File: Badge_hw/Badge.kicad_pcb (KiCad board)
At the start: 2 copper layers, 143 parts, among them Q1 IRLML9303, Q2 BC848

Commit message: +antenna
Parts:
- added D7: ANT, ANT_868_INV_F:ANTENNA_868_INV_F, F.Cu at (222.6, 22.6)
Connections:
- BLN1 pad 2: GNDS -> Net-(BLN1-Pad2)
- BLN1 pad 5: GNDS -> Net-(BLN1-Pad2)
- BLN1 pad 6: GNDS -> Net-(BLN1-Pad2)
- C14 pad 2: GNDS -> Net-(C14-Pad2)
- C15 pad 2: GNDS -> Net-(C15-Pad2)
- C16 pad 2: GNDS -> Net-(C16-Pad2)
- C19 pad 2: GNDS -> Net-(C15-Pad2)
- C20 pad 2: GNDS -> Net-(C20-Pad2)
- C3 pad 2: GNDS -> Net-(C15-Pad2)
- C31 pad 2: GNDS -> Net-(C31-Pad2)
- C32 pad 2: GNDS -> Net-(C32-Pad2)
- C33 pad 2: GNDS -> Net-(C33-Pad2)
- C34 pad 2: GNDS -> Net-(C34-Pad2)
- C35 pad 2: GNDS -> Net-(C35-Pad2)
- C36 pad 2: GNDS -> Net-(C36-Pad2)
- C37 pad 2: GNDS -> Net-(C37-Pad2)
- C38 pad 2: GNDS -> Net-(C38-Pad2)
- C39 pad 2: GNDS -> Net-(C39-Pad2)
- C40 pad 2: GNDS -> Net-(C40-Pad2)
- C41 pad 2: GNDS -> Net-(C41-Pad2)
- C42 pad 2: GNDS -> Net-(C42-Pad2)
- C43 pad 2: GNDS -> Net-(C43-Pad2)
- C44 pad 2: GNDS -> Net-(C44-Pad2)
- C45 pad 2: GNDS -> Net-(C45-Pad2)
- C47 pad 2: GNDS -> Net-(C47-Pad2)
- C48 pad 2: GNDS -> Net-(C48-Pad2)
- C50 pad 1: GNDS -> Net-(C50-Pad1)
- C51 pad 2: GNDS -> Net-(C51-Pad2)
- C53 pad 2: GNDS -> Net-(C53-Pad2)
- C54 pad 2: GNDS -> Net-(C54-Pad2)
- C55 pad 2: GNDS -> Net-(C55-Pad2)
- C56 pad 2: GNDS -> Net-(C56-Pad2)
- C57 pad 2: GNDS -> Net-(C57-Pad2)
- C59 pad 2: GNDS -> Net-(C59-Pad2)
- C60 pad 2: GNDS -> Net-(C60-Pad2)
- C61 pad 2: GNDS -> Net-(C61-Pad2)
- C62 pad 2: GNDS -> Net-(C62-Pad2)
- C63 pad 2: GNDS -> Net-(C63-Pad2)
- C64 pad 2: GNDS -> Net-(C64-Pad2)
- C65 pad 2: GNDS -> Net-(C65-Pad2)
- C66 pad 2: GNDS -> Net-(C66-Pad2)
- C9 pad 2: GNDS -> Net-(C15-Pad2)
- D2 pad C: GNDS -> Net-(D2-PadC)
- D4 pad 1: GNDS -> Net-(D4-Pad1)
- D4 pad 2: GNDS -> Net-(D4-Pad1)
- D4 pad 3: GNDS -> Net-(D4-Pad1)
- DA1 pad 4: GNDS -> Net-(DA1-Pad4)
- DD1 pad 10: GNDS -> Net-(DD1-Pad10)
- DD1 pad 3: GNDS -> Net-(DD1-Pad3)
- DD1 pad 9: GNDS -> Net-(DD1-Pad9)
- DD2 pad 11: GNDS -> Net-(DD2-Pad11)
- DD2 pad 12: GNDS -> Net-(DD2-Pad11)
- DD2 pad 13: GNDS -> Net-(DD2-Pad11)
- DD2 pad 14: GNDS -> Net-(DD2-Pad11)
- DD2 pad 15: GNDS -> Net-(DD2-Pad15)
- DD2 pad 16: GNDS -> Net-(DD2-Pad15)
- DD2 pad 34: GNDS -> Net-(DD2-Pad34)
- DD2 pad 7: GNDS -> Net-(DD2-Pad11)
- DD2 pad 9: GNDS -> Net-(DD2-Pad11)
- DD4 pad 10: GNDS -> Net-(DD4-Pad10)
- DD4 pad 19: GNDS -> Net-(DD4-Pad19)
- DD4 pad 20: GNDS -> Net-(DD4-Pad20)
- DD4 pad 27: GNDS -> Net-(DD4-Pad10)
- DD4 pad 49: GNDS -> Net-(DD4-Pad10)
- DD4 pad 74: GNDS -> Net-(DD4-Pad10)
- DD4 pad 99: GNDS -> Net-(DD4-Pad10)
- DD5 pad 16: GNDS -> Net-(DD5-Pad16)
- DD5 pad 19: GNDS -> Net-(DD5-Pad16)
- DD5 pad PAD: GNDS -> Net-(DD5-PadPAD)
- L6 pad 2: GNDS -> Net-(L6-Pad2)
- Q2 pad 2: GNDS -> Net-(Q2-Pad2)
- R34 pad 1: GNDS -> Net-(R34-Pad1)
- R35 pad 2: GNDS -> Net-(R35-Pad2)
- R36 pad 1: GNDS -> Net-(R36-Pad1)
- R40 pad 2: GNDS -> Net-(R40-Pad2)
- R42 pad 1: GNDS -> Net-(R42-Pad1)
- R46 pad 2: GNDS -> Net-(R46-Pad2)
- SA2 pad 1: GNDS -> Net-(SA2-Pad1)
- XL3 pad 6: GNDS -> Net-(XL3-Pad6)
- XL3 pad H: GNDS -> Net-(XL3-PadH)
- XTAL1 pad H: GNDS -> Net-(XTAL1-PadH)
- XTAL2 pad H: GNDS -> Net-(XTAL2-PadH)

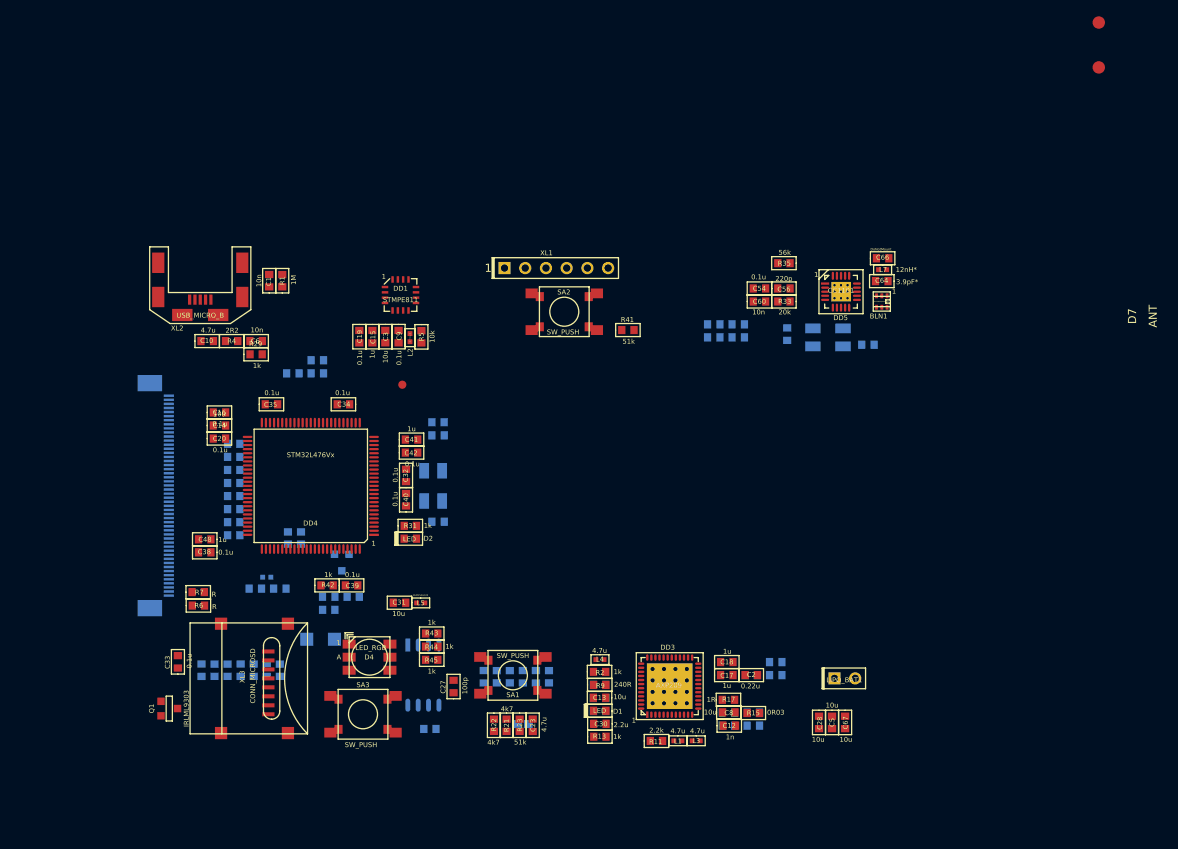
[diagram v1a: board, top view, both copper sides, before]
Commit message: * pcb redraw + barometer scheme
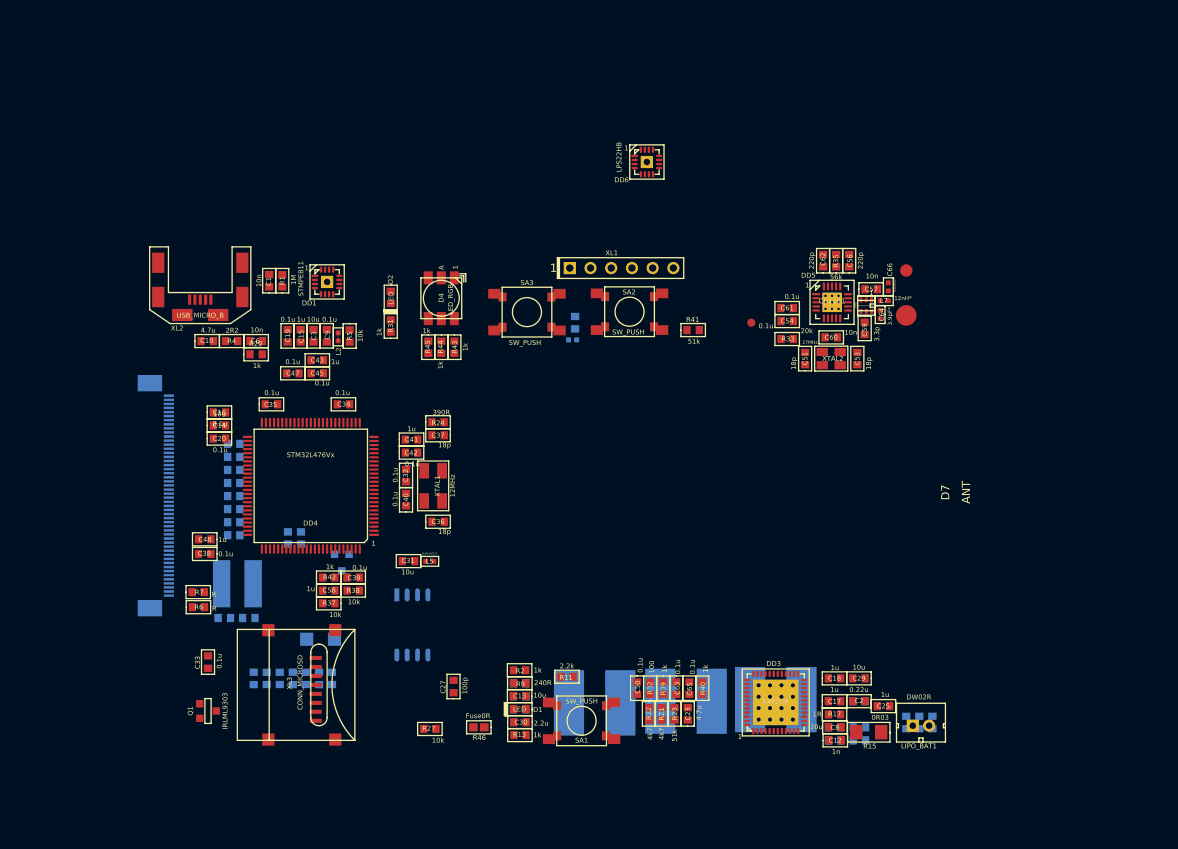
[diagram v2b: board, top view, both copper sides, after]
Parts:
- added C68: 0.1u, Capacitors:CAP_0603, B.Cu at (158.4, 59.4)
- added DD6: LPS22HB, QFN_DFN:QFN16_4x4_H, F.Cu at (167.2, 39.7)
- added L8: BLM15AG102, Inductors:IND_0402, B.Cu at (158.1, 61.5)
- C25, C29, C36, C37, C43, C45, C47, C50, C51, C53, C57, C58, C59, C61, C62, C63, C65, R24, R27, R32, R37, R38, R39, R40, R46, XTAL1: moved to F.Cu
- C28, C5, C67: moved to B.Cu
- C64, C66: footprint Capacitors:CAP_0603 -> Capacitors:CAP_0402
- D7: footprint ANT_868_INV_F:ANTENNA_868_INV_F -> ANT_868_INV_F:ANTENNA_868_INV_F_SHARP
- DD1: footprint LGA:16_4X4_P065 -> QFN_DFN:QFN16_4x4_H
- L1, L3, L4: footprint Inductors:IND_0402 -> Inductors:SDR0805; moved to B.Cu
- L6: footprint Inductors:IND_0402 -> Inductors:IND_SDR0604
- LIPO_BAT1: footprint Connectors:PLS-2 -> Connectors:WB-02(MW-2M)
- R15: footprint Resistors:RES_0603 -> Resistors:RES_1206
- XTAL2: footprint Quartz:0503x4-4 -> Quartz:03225C4; moved to F.Cu
- moved SA3 53.2 mm to (152.5, 58.1)
- moved D4 44.9 mm to (142.0, 56.4), turned to 270 degrees
- moved TP1 43.4 mm to (180.0, 59.4)
- moved R45 38.3 mm to (140.4, 62.4), turned to 270 degrees
- moved D7 38.0 mm to (199.8, 53.0)
- moved R44 36.7 mm to (142.0, 62.4), turned to 270 degrees
- moved R43 35.2 mm to (143.6, 62.4), turned to 270 degrees
- moved D2 29.7 mm to (135.8, 56.3), turned to 270 degrees
- moved R31 24.6 mm to (135.8, 59.8), turned to 90 degrees
- moved L4 22.1 mm to (183.0, 105.6), turned to 90 degrees
- moved C57 19.8 mm to (194.7, 55.3)
- moved C23 19.1 mm to (172.2, 107.3)
- moved R21 19.1 mm to (169.0, 107.3)
- moved R22 19.1 mm to (167.4, 107.3)
- moved R23 19.1 mm to (170.6, 107.3)
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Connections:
- C1 pad 2: GND -> Net-(C1-Pad2)
- C10 pad 1: GND -> Net-(C10-Pad1)
- C11 pad 2: GND -> Net-(C11-Pad2)
- C12 pad 2: GND -> Net-(C12-Pad2)
- C13 pad 2: GND -> Net-(C13-Pad2)
- C17 pad 2: GND -> Net-(C17-Pad2)
- C18 pad 2: GND -> Net-(C18-Pad2)
- C2 pad 2: GND -> Net-(C2-Pad2)
- C21 pad 2: GND -> Net-(C21-Pad2)
- C22 pad 2: GND -> Net-(C22-Pad2)
- C23 pad 1: +3V3 -> +3V3_120mA
- C23 pad 2: GND -> Net-(C23-Pad2)
- C24 pad 2: GND -> Net-(C24-Pad2)
- C25 pad 2: GND -> Net-(C25-Pad2)
- C26 pad 2: GND -> Net-(C26-Pad2)
- C27 pad 2: GND -> Net-(C27-Pad2)
- C28 pad 2: GND -> Net-(C28-Pad2)
- C29 pad 1: GND -> Net-(C29-Pad1)
- C30 pad 2: GND -> Net-(C30-Pad2)
- C4 pad 2: GND -> Net-(C4-Pad2)
- C5 pad 2: GND -> Net-(C5-Pad2)
- C6 pad 2: GND -> Net-(C6-Pad2)
- C67 pad 2: GND -> Net-(C5-Pad2)
- C7 pad 2: GND -> Net-(C7-Pad2)
- C8 pad 2: GND -> Net-(C8-Pad2)
- DD2 pad 1: +3V3 -> +3V3_120mA
- DD2 pad 43: GND -> Net-(DD2-Pad43)
- DD2 pad 48: GND -> Net-(DD2-Pad43)
- DD2 pad 49: GND -> Net-(DD2-Pad43)
- DD2 pad 50: GND -> Net-(DD2-Pad43)
- DD3 pad 12: +3V3 -> +3V3_120mA
- DD3 pad 16: GND -> Net-(DD3-Pad16)
- DD3 pad 22: GND -> Net-(DD3-Pad22)
- DD3 pad 46: GND -> Net-(DD3-Pad46)
- DD3 pad 6: GND -> Net-(DD3-Pad6)
- DD3 pad 9: GND -> Net-(DD3-Pad9)
- DD3 pad PAD: GND -> Net-(DD3-PadPAD)
- DD4 pad 81: Net-(DD4-Pad81) -> /PRESSURE_INT
- LIPO_BAT1 pad 2: GND -> Net-(C5-Pad2)
- R1 pad 2: GND -> Net-(R1-Pad2)
- R11 pad 1: GND -> Net-(R11-Pad1)
- R3 pad 2: GND -> Net-(R3-Pad2)
- R46 pad 1: GND -> Net-(R46-Pad1)
- R6 pad 2: +3V3 -> +3V3_120mA
- R7 pad 2: +3V3 -> +3V3_120mA
- R9 pad 1: GND -> Net-(R9-Pad1)
- SA1 pad 2: GND -> Net-(SA1-Pad2)
- XL1 pad 3: GND -> Net-(XL1-Pad3)
- XL2 pad 4: GND -> Net-(XL2-Pad4)
- XL2 pad 5: GND -> Net-(XL2-Pad4)

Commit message: * schematic, footprints
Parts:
- C44: value 150pF -> 150p
- C49: value 100pF -> 100p
- C64: value 3.9pF* -> 3.9p*
- DA1: footprint SO_DIL_TSSOP:SO8_208MIL -> SOT:SOT23-8
- DD6: footprint QFN_DFN:QFN16_4x4_H -> LGA:10_2X2
- L1, L3, L4: value 4.7u -> 4.7uH; footprint Inductors:SDR0805 -> Inductors:IND_SDR0604
- L6: footprint Inductors:IND_SDR0604 -> Inductors:IND_1812
- R15: footprint Resistors:RES_1206 -> Resistors:RES_2512
- moved DD6 40.8 mm to (136.0, 66.0)
- moved LIPO_BAT1 9.95 mm to (192.2, 103.8)
- moved C25 9.11 mm to (187.6, 103.4)
- moved R46 9.02 mm to (137.6, 108.4)
- moved DD3 9.01 mm to (174.0, 106.4)
- moved D1 8.80 mm to (142.8, 106.8)
- moved R9 8.80 mm to (142.8, 103.6)
- moved C13 8.80 mm to (142.8, 105.2)
- moved C24 8.80 mm to (142.8, 103.6)
- moved C26 8.80 mm to (142.8, 105.2)
- moved C30 8.80 mm to (142.8, 108.4)
- moved C7 8.80 mm to (142.8, 106.8)
- moved R13 8.80 mm to (142.8, 110.0)
- moved R2 8.80 mm to (142.8, 102.0)
- moved C17 8.61 mm to (181.6, 106.2)
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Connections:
- BLN1 pad 2: Net-(BLN1-Pad2) -> GNDS
- BLN1 pad 5: Net-(BLN1-Pad2) -> GNDS
- BLN1 pad 6: Net-(BLN1-Pad2) -> GNDS
- C1 pad 2: Net-(C1-Pad2) -> GNDA
- C10 pad 1: Net-(C10-Pad1) -> GNDA
- C11 pad 2: Net-(C11-Pad2) -> GNDA
- C12 pad 2: Net-(C12-Pad2) -> GNDA
- C13 pad 2: Net-(C13-Pad2) -> GNDA
- C14 pad 2: Net-(C14-Pad2) -> GNDS
- C16 pad 2: Net-(C16-Pad2) -> GNDS
- C17 pad 2: Net-(C17-Pad2) -> GNDA
- C18 pad 2: Net-(C18-Pad2) -> GNDA
- C2 pad 2: Net-(C2-Pad2) -> GNDA
- C20 pad 2: Net-(C20-Pad2) -> GNDS
- C21 pad 2: Net-(C21-Pad2) -> GNDA
- C22 pad 2: Net-(C22-Pad2) -> GNDA
- C23 pad 2: Net-(C23-Pad2) -> GNDA
- C24 pad 2: Net-(C24-Pad2) -> GNDA
- C25 pad 2: Net-(C25-Pad2) -> GNDA
- C26 pad 2: Net-(C26-Pad2) -> GNDA
- C27 pad 2: Net-(C27-Pad2) -> GNDA
- C28 pad 2: Net-(C28-Pad2) -> GNDA
- C29 pad 1: Net-(C29-Pad1) -> GNDA
- C30 pad 2: Net-(C30-Pad2) -> GNDA
- C31 pad 2: Net-(C31-Pad2) -> GNDS
- C32 pad 2: Net-(C32-Pad2) -> GNDS
- C33 pad 2: Net-(C33-Pad2) -> GNDS
- C34 pad 2: Net-(C34-Pad2) -> GNDS
- C35 pad 2: Net-(C35-Pad2) -> GNDS
- C36 pad 2: Net-(C36-Pad2) -> GNDS
- C37 pad 2: Net-(C37-Pad2) -> GNDS
- C38 pad 2: Net-(C38-Pad2) -> GNDS
- C39 pad 2: Net-(C39-Pad2) -> GNDS
- C4 pad 2: Net-(C4-Pad2) -> GNDA
- C40 pad 2: Net-(C40-Pad2) -> GNDS
- C41 pad 2: Net-(C41-Pad2) -> GNDS
- C42 pad 2: Net-(C42-Pad2) -> GNDS
- C43 pad 2: Net-(C43-Pad2) -> GNDS
- C44 pad 2: Net-(C44-Pad2) -> GNDS
- C45 pad 2: Net-(C45-Pad2) -> GNDS
- C47 pad 2: Net-(C47-Pad2) -> GNDS
- C48 pad 2: Net-(C48-Pad2) -> GNDS
- C5 pad 2: Net-(C5-Pad2) -> GNDA
- C50 pad 1: Net-(C50-Pad1) -> GNDS
- C51 pad 2: Net-(C51-Pad2) -> GNDS
- C53 pad 2: Net-(C53-Pad2) -> GNDS
- C54 pad 2: Net-(C54-Pad2) -> GNDS
- C55 pad 2: Net-(C55-Pad2) -> GNDS
- C56 pad 2: Net-(C56-Pad2) -> GNDS
- C57 pad 2: Net-(C57-Pad2) -> GNDS
- C59 pad 2: Net-(C59-Pad2) -> GNDS
- C6 pad 2: Net-(C6-Pad2) -> GNDA
- C60 pad 2: Net-(C60-Pad2) -> GNDS
- C61 pad 2: Net-(C61-Pad2) -> GNDS
- C62 pad 2: Net-(C62-Pad2) -> GNDS
- C63 pad 2: Net-(C63-Pad2) -> GNDS
- C64 pad 2: Net-(C64-Pad2) -> GNDS
- C65 pad 2: Net-(C65-Pad2) -> GNDS
- C66 pad 2: Net-(C66-Pad2) -> GNDS
- C67 pad 2: Net-(C5-Pad2) -> GNDA
- C68 pad 2: Net-(C68-Pad2) -> GNDS
- C7 pad 2: Net-(C7-Pad2) -> GNDA
- C8 pad 2: Net-(C8-Pad2) -> GNDA
- D2 pad C: Net-(D2-PadC) -> GNDS
- D4 pad 1: Net-(D4-Pad1) -> GNDS
- D4 pad 2: Net-(D4-Pad1) -> GNDS
- D4 pad 3: Net-(D4-Pad1) -> GNDS
- D7 pad GND: Net-(D7-PadGND) -> GNDS
- DD1 pad 10: Net-(DD1-Pad10) -> GNDS
- DD1 pad 3: Net-(DD1-Pad3) -> GNDS
- DD1 pad 9: Net-(DD1-Pad9) -> GNDS
- DD2 pad 11: Net-(DD2-Pad11) -> GNDS
- DD2 pad 12: Net-(DD2-Pad11) -> GNDS
- DD2 pad 13: Net-(DD2-Pad11) -> GNDS
- DD2 pad 14: Net-(DD2-Pad11) -> GNDS
- DD2 pad 15: Net-(DD2-Pad15) -> GNDS
- DD2 pad 16: Net-(DD2-Pad15) -> GNDS
- DD2 pad 34: Net-(DD2-Pad34) -> GNDS
- DD2 pad 43: Net-(DD2-Pad43) -> GNDA
- DD2 pad 48: Net-(DD2-Pad43) -> GNDA
- DD2 pad 49: Net-(DD2-Pad43) -> GNDA
- DD2 pad 50: Net-(DD2-Pad43) -> GNDA
- DD2 pad 7: Net-(DD2-Pad11) -> GNDS
- DD2 pad 9: Net-(DD2-Pad11) -> GNDS
- DD3 pad 16: Net-(DD3-Pad16) -> GNDA
- DD3 pad 22: Net-(DD3-Pad22) -> GNDA
- DD3 pad 46: Net-(DD3-Pad46) -> GNDA
- DD3 pad 6: Net-(DD3-Pad6) -> GNDA
- DD3 pad 9: Net-(DD3-Pad9) -> GNDA
- DD3 pad PAD: Net-(DD3-PadPAD) -> GNDA
- DD4 pad 10: Net-(DD4-Pad10) -> GNDS
- DD4 pad 19: Net-(DD4-Pad19) -> GNDS
- DD4 pad 20: Net-(DD4-Pad20) -> GNDS
- DD4 pad 27: Net-(DD4-Pad10) -> GNDS
- DD4 pad 49: Net-(DD4-Pad10) -> GNDS
- DD4 pad 74: Net-(DD4-Pad10) -> GNDS
- DD4 pad 99: Net-(DD4-Pad10) -> GNDS
- DD5 pad 16: Net-(DD5-Pad16) -> GNDS
- DD5 pad 19: Net-(DD5-Pad16) -> GNDS
- DD5 pad PAD: Net-(DD5-PadPAD) -> GNDS
- DD6 pad 3: Net-(DD6-Pad3) -> GNDS
- DD6 pad 5: Net-(DD6-Pad3) -> GNDS
- DD6 pad 8: Net-(DD6-Pad8) -> GNDS
- DD6 pad 9: Net-(DD6-Pad8) -> GNDS
- L6 pad 2: Net-(L6-Pad2) -> GNDS
- LIPO_BAT1 pad 2: Net-(C5-Pad2) -> GNDA
- Q2 pad 2: Net-(Q2-Pad2) -> GNDS
- R1 pad 2: Net-(R1-Pad2) -> GNDA
- R11 pad 1: Net-(R11-Pad1) -> GNDA
- R3 pad 2: Net-(R3-Pad2) -> GNDA
- R34 pad 1: Net-(R34-Pad1) -> GNDS
- R35 pad 2: Net-(R35-Pad2) -> GNDS
- R36 pad 1: Net-(R36-Pad1) -> GNDS
- R40 pad 2: Net-(R40-Pad2) -> GNDS
- R42 pad 1: Net-(R42-Pad1) -> GNDS
- R46 pad 1: Net-(R46-Pad1) -> GNDA
- R46 pad 2: Net-(R46-Pad2) -> GNDS
- R9 pad 1: Net-(R9-Pad1) -> GNDA
- SA1 pad 2: Net-(SA1-Pad2) -> GNDA
- SA2 pad 1: Net-(SA2-Pad1) -> GNDS
- XL1 pad 3: Net-(XL1-Pad3) -> GNDA
- XL2 pad 4: Net-(XL2-Pad4) -> GNDA
- XL2 pad 5: Net-(XL2-Pad4) -> GNDA
- XL3 pad 6: Net-(XL3-Pad6) -> GNDS
- XL3 pad H: Net-(XL3-PadH) -> GNDS
- XTAL1 pad H: Net-(XTAL1-PadH) -> GNDS
- XTAL2 pad H: Net-(XTAL2-PadH) -> GNDS
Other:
- board outline added: 114 x 62 mm

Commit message: +pcb
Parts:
- C1, C10, C13, C17, C18, C2, C23, C25, C27, C29, C30, C6, C63, C65, D1, DD3, LIPO_BAT1, R1, R11, R13, R15, R17, R2, R21, R22, R23, R29, R39, R4, R40, R46, R9, SA2, SA3, XL2: moved to B.Cu
- C11, C4, C44, C46, C49, C52, C55, D3, DA1, L1, L3, L4, L6, Q2, R25, R26, R28, R30, R34, R36: moved to F.Cu
- moved C44 72.0 mm to (189.0, 109.7)
- moved C46 72.0 mm to (186.0, 109.7)
- moved R15 66.0 mm to (130.8, 81.6)
- moved C25 64.9 mm to (123.0, 97.4)
- moved C67 63.2 mm to (134.5, 88.0), turned to 0 degrees
- moved C49 62.8 mm to (181.2, 111.1), turned to 0 degrees
- moved C5 62.4 mm to (134.5, 86.4), turned to 0 degrees
- moved C19 61.9 mm to (162.6, 108.7)
- moved C28 61.5 mm to (134.5, 84.9), turned to 0 degrees
- moved C15 61.1 mm to (162.6, 108.9)
- moved R28 61.0 mm to (181.2, 109.5), turned to 0 degrees
- moved R3 59.4 mm to (128.2, 105.2), turned to 270 degrees
- moved C22 59.3 mm to (125.6, 89.8)
- moved R30 59.2 mm to (181.2, 107.9), turned to 0 degrees
- moved C31 58.8 mm to (194.6, 104.4)
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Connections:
- DD3 pad 2: /SCK -> /SCL
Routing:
- net GNDA: track 0.00 -> 120.4 mm, vias 0 -> 10
- net /PWR_UNST: track 0.00 -> 58.9 mm, vias 0 -> 9
- net +BATT: track 0.00 -> 38.0 mm, vias 0 -> 4
- net Net-(C1-Pad1): track 0.00 -> 31.9 mm
- net +3V3: track 0.00 -> 27.9 mm, vias 0 -> 2
- net +5V: track 0.00 -> 22.5 mm, vias 0 -> 3
- net Net-(C24-Pad1): track 0.00 -> 18.1 mm, vias 0 -> 1
- net Net-(C27-Pad1): track 0.00 -> 13.9 mm, vias 0 -> 2
- net Net-(DD3-Pad45): track 0.00 -> 12.8 mm, vias 0 -> 1
- net /PWR_IRQ: track 0.00 -> 11.5 mm, vias 0 -> 2
- net /SDA: track 0.00 -> 10.5 mm, vias 0 -> 2
- net /DCDC_2: track 0.00 -> 10.1 mm, vias 0 -> 1
- net /SCL: track 0.00 -> 8.38 mm
- net /LDO_3: track 0.00 -> 7.65 mm
- net Net-(DD3-Pad47): track 0.00 -> 6.81 mm
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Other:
- net class Default: trace_width 0.15 -> 0.2; via_dia 0.5 -> 0.7
- net class power: trace_width 0.2 -> 0.5; via_dia 0.5 -> 0.7

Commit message: pcb full 1.0
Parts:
- C15, C19, C3, C32, C33, C34, C35, C36, C37, C38, C39, C40, C41, C42, C43, C45, C47, C48, C9, D2, D4, DD1, DD4, DD6, L2, Q1, R24, R31, R41, R42, R43, R44, R45, R5, TP1, XL3, XTAL1: moved to B.Cu
- DD2, R10, R12, R14, R16, R18, R19, R20, R8: moved to F.Cu
- moved R41 73.2 mm to (104.8, 63.6), turned to 180 degrees
- moved SA2 71.5 mm to (105.2, 69.4), turned to 270 degrees
- moved L5 64.0 mm to (137.4, 77.6)
- moved C31 62.1 mm to (137.6, 79.8), turned to 270 degrees
- moved C39 61.7 mm to (119.2, 85.4), turned to 270 degrees
- moved SA3 61.1 mm to (107.4, 78.0)
- moved R42 57.2 mm to (121.0, 85.4), turned to 90 degrees
- moved C68 56.8 mm to (152.8, 108.2)
- moved C15 56.7 mm to (108.6, 91.6)
- moved R5 55.7 mm to (112.6, 89.2), turned to 0 degrees
- moved XL3 55.7 mm to (154.8, 57.8)
- moved C19 55.1 mm to (110.2, 91.6)
- moved L8 54.5 mm to (150.6, 106.2), turned to 0 degrees
- moved C9 53.2 mm to (111.8, 91.6)
- moved D4 52.6 mm to (115.4, 76.8), turned to 90 degrees
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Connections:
- C15 pad 2: Net-(C15-Pad2) -> GNDS
- C19 pad 2: Net-(C15-Pad2) -> GNDS
- C3 pad 2: Net-(C15-Pad2) -> GNDS
- C9 pad 2: Net-(C15-Pad2) -> GNDS
- DD2 pad 43: GNDA -> GNDS
- DD2 pad 48: GNDA -> GNDS
- DD2 pad 49: GNDA -> GNDS
- DD2 pad 50: GNDA -> GNDS
- DD4 pad 15: /SCK -> /SCL
- DD4 pad 67: /CHARGING -> Net-(DD4-Pad67)
- XL1 pad 3: GNDA -> GNDS
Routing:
- net +3V3: track 27.9 -> 422.7 mm, vias 2 -> 24
- net GNDS: track 0.00 -> 387.4 mm, vias 0 -> 27
- net /CC_GDO0: track 0.00 -> 82.6 mm, vias 0 -> 3
- net /CC_CS: track 0.00 -> 78.1 mm, vias 0 -> 1
- net /klNFC_Tx: track 0.00 -> 78.0 mm, vias 0 -> 3
- net /CC_SCK: track 0.00 -> 72.0 mm, vias 0 -> 1
- net /klNFC_Rx: track 0.00 -> 71.9 mm, vias 0 -> 3
- net /CC_MISO: track 0.00 -> 71.0 mm, vias 0 -> 1
- net /CC_MOSI: track 0.00 -> 70.9 mm, vias 0 -> 1
- net /UART_RX: track 0.00 -> 63.3 mm, vias 0 -> 2
- net /UART_TX: track 0.00 -> 63.1 mm, vias 0 -> 2
- net /SWD_IO: track 0.00 -> 53.0 mm, vias 0 -> 1
- net /PRESSURE_INT: track 0.00 -> 52.2 mm, vias 0 -> 2
- net /SWD_CLK: track 0.00 -> 50.3 mm, vias 0 -> 1
- net /SCL: track 8.38 -> 58.6 mm, vias 0 -> 2
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
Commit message: *pcb 2.0
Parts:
- added G***: LOGO, Badge_hw:logo, B.Cu at (207.8, 80.7)
- C33, Q1, R24, R43, R44, R45: moved to F.Cu
- moved C44 24.6 mm to (194.4, 107.4)
- moved L6 24.6 mm to (191.8, 107.2)
- moved C46 21.1 mm to (183.6, 105.0)
- moved C49 21.1 mm to (181.0, 107.4)
- moved R25 21.1 mm to (182.6, 107.4)
- moved R27 21.1 mm to (185.8, 107.4)
- moved R28 21.1 mm to (184.2, 107.4)
- moved R30 12.8 mm to (176.6, 108.0)
- moved DA1 10.2 mm to (170.8, 106.8)
- moved R26 10.2 mm to (167.6, 106.0)
- moved C68 9.73 mm to (162.5, 107.1)
- moved L8 9.14 mm to (159.6, 104.7)
- moved C52 9.06 mm to (165.6, 109.8)
- moved C55 9.06 mm to (162.6, 107.8)
- moved D3 9.06 mm to (161.4, 109.6)
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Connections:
- C31 pad 1: +3V3 -> MCU_PWR
- C32 pad 1: +3V3 -> MCU_PWR
- C34 pad 1: +3V3 -> MCU_PWR
- C35 pad 1: +3V3 -> MCU_PWR
- C38 pad 1: +3V3 -> MCU_PWR
- C39 pad 1: +3V3 -> MCU_PWR
- C40 pad 1: +3V3 -> MCU_PWR
- C41 pad 1: +3V3 -> MCU_PWR
- C42 pad 1: +3V3 -> MCU_PWR
- C43 pad 1: +3V3 -> MCU_PWR
- C45 pad 1: +3V3 -> MCU_PWR
- C47 pad 1: +3V3 -> MCU_PWR
- C48 pad 1: +3V3 -> MCU_PWR
- DD4 pad 100: +3V3 -> MCU_PWR
- DD4 pad 11: +3V3 -> MCU_PWR
- DD4 pad 21: +3V3 -> MCU_PWR
- DD4 pad 22: +3V3 -> MCU_PWR
- DD4 pad 28: +3V3 -> MCU_PWR
- DD4 pad 50: +3V3 -> MCU_PWR
- DD4 pad 6: +3V3 -> MCU_PWR
- DD4 pad 73: +3V3 -> MCU_PWR
- DD4 pad 75: +3V3 -> MCU_PWR
- L5 pad 1: +3V3 -> MCU_PWR
- R41 pad 2: +3V3 -> MCU_PWR
- SA3 pad 2: +3V3 -> MCU_PWR
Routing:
- net MCU_PWR: track 0.00 -> 178.0 mm, vias 0 -> 9
- net +3V3: track 422.7 -> 297.0 mm, vias 24 -> 19
- net GNDS: track 387.4 -> 495.3 mm, vias 27 -> 31
- net /TOUCH_INT: track 0.00 -> 73.7 mm, vias 0 -> 2
- net /SCL: track 58.6 -> 126.0 mm, vias 2 -> 5
- net /SDA: track 55.1 -> 121.5 mm, vias 5 -> 7
- net /klNFC_Tx: track 78.0 -> 100.6 mm
- net VGND: track 27.2 -> 48.2 mm, vias 3 -> 2
- net Net-(DA1-Pad2): track 5.84 -> 18.4 mm
- net /SD_DAT1: track 38.6 -> 27.5 mm, vias 0 -> 2
- net Net-(C49-Pad2): track 4.35 -> 15.0 mm, vias 0 -> 2
- net Net-(C50-Pad2): track 16.7 -> 26.9 mm, vias 2 -> 0
- net Net-(DD4-Pad2): track 3.33 -> 13.4 mm, vias 0 -> 1
- net Net-(DD4-Pad3): track 3.86 -> 13.2 mm, vias 0 -> 1
- net Net-(DD4-Pad4): track 5.02 -> 13.0 mm, vias 0 -> 1
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- added copper zone on B.Cu, net GNDS
- added copper zone on F.Cu, net GNDS
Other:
- outline, holes or cut-outs redrawn
- rule via_min_size: 0.4 -> 0.7
